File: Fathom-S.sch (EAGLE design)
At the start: 107 parts, among them IC1 LMH6643, IC2 LMH6643, IC3 ST490AB, IC4 ST490AB, IC5 FT230XS, Q1 BC817-40W, U1 MC7812, U2 MC7805, U4 INA139, U5 MC7805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

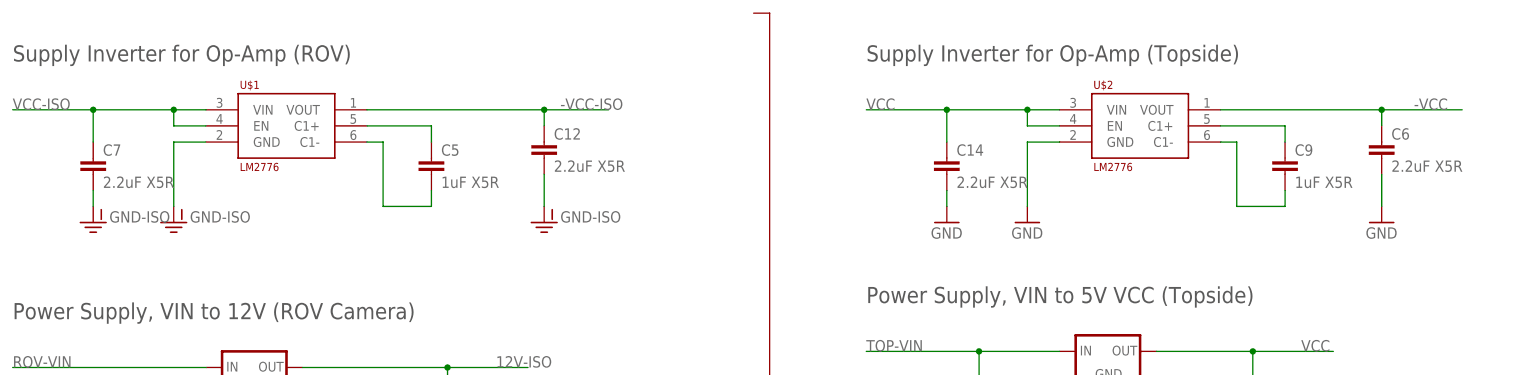
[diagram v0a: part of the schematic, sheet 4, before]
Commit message: Changed lm2776 components to match datasheet and hopefully fix our issues.
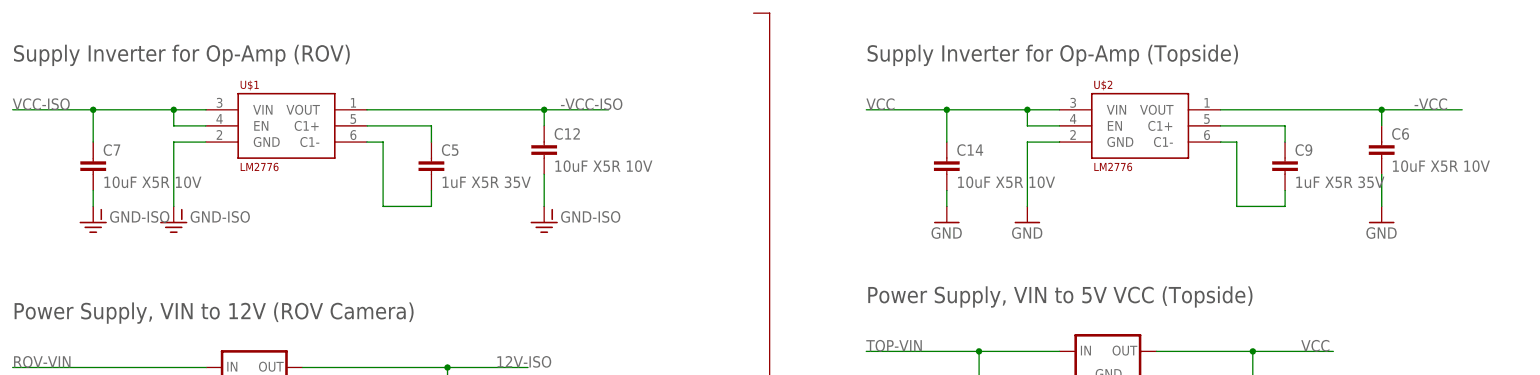
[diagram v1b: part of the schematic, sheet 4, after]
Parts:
- C12, C14, C6, C7: value 2.2uF X5R -> 10uF X5R 10V
- C5, C9: value 1uF X5R -> 1uF X5R 35V
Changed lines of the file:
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@@
 <part name="JP1" library="BR-Eagle-Library" deviceset="RCA" device="" value="PJRAN1X1U04X"/>
 <part name="U$1" library="BR-Eagle-Library" deviceset="LM2776" device=""/>
-<part name="C5" library="SparkFun-Passives" deviceset="CAP" device="0603-CAP" value="1uF X5R"/>
-<part name="C7" library="SparkFun-Passives" deviceset="CAP" device="0603-CAP" value="2.2uF X5R"/>
+<part name="C5" library="SparkFun-Passives" deviceset="CAP" device="0603-CAP" value="1uF X5R 35V"/>
+<part name="C7" library="SparkFun-Passives" deviceset="CAP" device="0603-CAP" value="10uF X5R 10V"/>
 <part name="C8" library="SparkFun-Passives" deviceset="CAP" device="0603-CAP" value="0.1uF"/>
 <part name="C10" library="SparkFun-Passives" deviceset="CAP_POL" device="1206" value="10uF 16V"/>
@@
 <part name="JP6" library="BR-Eagle-Library" deviceset="RCA" device="" value="PJRAN1X1U04X"/>
 <part name="U$2" library="BR-Eagle-Library" deviceset="LM2776" device=""/>
-<part name="C9" library="SparkFun-Passives" deviceset="CAP" device="0603-CAP" value="1uF X5R"/>
-<part name="C14" library="SparkFun-Passives" deviceset="CAP" device="0603-CAP" value="2.2uF X5R"/>
+<part name="C9" library="SparkFun-Passives" deviceset="CAP" device="0603-CAP" value="1uF X5R 35V"/>
+<part name="C14" library="SparkFun-Passives" deviceset="CAP" device="0603-CAP" value="10uF X5R 10V"/>
 <part name="GND12" library="SparkFun-Aesthetics" deviceset="GND" device=""/>
 <part name="GND13" library="SparkFun-Aesthetics" deviceset="GND" device=""/>
@@
 <part name="R17" library="SparkFun" deviceset="RESISTOR" device="0603-RES" value="10K"/>
 <part name="SJ4" library="SparkFun-Passives" deviceset="JUMPER-PAD-2-NC_BY_PASTE" device=""/>
-<part name="C6" library="SparkFun-Passives" deviceset="CAP" device="0603-CAP" value="2.2uF X5R"/>
-<part name="C12" library="SparkFun-Passives" deviceset="CAP" device="0603-CAP" value="2.2uF X5R"/>
+<part name="C6" library="SparkFun-Passives" deviceset="CAP" device="0603-CAP" value="10uF X5R 10V"/>
+<part name="C12" library="SparkFun-Passives" deviceset="CAP" device="0603-CAP" value="10uF X5R 10V"/>
 </parts>
 <sheets>

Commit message: Layout 'typos' fixed.
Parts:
- C12, C14, C6, C7: device SparkFun-Passives:CAP0603-CAP -> SparkFun-Passives:CAP0805
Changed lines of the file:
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@@
 <grid distance="0.1" unitdist="inch" unit="inch" style="lines" multiple="1" display="no" altdistance="0.01" altunitdist="inch" altunit="inch"/>
 <layers>
-<layer number="1" name="Top" color="4" fill="1" visible="no" active="no"/>
-<layer number="2" name="Route2" color="1" fill="3" visible="no" active="no"/>
-<layer number="3" name="Route3" color="4" fill="3" visible="no" active="no"/>
-<layer number="14" name="Route14" color="1" fill="6" visible="no" active="no"/>
-<layer number="15" name="Route15" color="4" fill="6" visible="no" active="no"/>
-<layer number="16" name="Bottom" color="1" fill="1" visible="no" active="no"/>
-<layer number="17" name="Pads" color="2" fill="1" visible="no" active="no"/>
-<layer number="18" name="Vias" color="2" fill="1" visible="no" active="no"/>
-<layer number="19" name="Unrouted" color="6" fill="1" visible="no" active="no"/>
-<layer number="20" name="Dimension" color="15" fill="1" visible="no" active="no"/>
-<layer number="21" name="tPlace" color="7" fill="1" visible="no" active="no"/>
-<layer number="22" name="bPlace" color="7" fill="1" visible="no" active="no"/>
-<layer number="23" name="tOrigins" color="15" fill="1" visible="no" active="no"/>
-<layer number="24" name="bOrigins" color="15" fill="1" visible="no" active="no"/>
-<layer number="25" name="tNames" color="7" fill="1" visible="no" active="no"/>
-<layer number="26" name="bNames" color="7" fill="1" visible="no" active="no"/>
-<layer number="27" name="tValues" color="7" fill="1" visible="no" active="no"/>
-<layer number="28" name="bValues" color="7" fill="1" visible="no" active="no"/>
+<layer number="1" name="Top" color="4" fill="1" visible="yes" active="no"/>
+<layer number="2" name="Route2" color="1" fill="3" visible="yes" active="no"/>
+<layer number="3" name="Route3" color="4" fill="3" visible="yes" active="no"/>
+<layer number="14" name="Route14" color="1" fill="6" visible="yes" active="no"/>
+<layer number="15" name="Route15" color="4" fill="6" visible="yes" active="no"/>
+<layer number="16" name="Bottom" color="1" fill="1" visible="yes" active="no"/>
+<layer number="17" name="Pads" color="2" fill="1" visible="yes" active="no"/>
+<layer number="18" name="Vias" color="2" fill="1" visible="yes" active="no"/>
+<layer number="19" name="Unrouted" color="6" fill="1" visible="yes" active="no"/>
+<layer number="20" name="Dimension" color="15" fill="1" visible="yes" active="no"/>
+<layer number="21" name="tPlace" color="7" fill="1" visible="yes" active="no"/>
+<layer number="22" name="bPlace" color="7" fill="1" visible="yes" active="no"/>
+<layer number="23" name="tOrigins" color="15" fill="1" visible="yes" active="no"/>
+<layer number="24" name="bOrigins" color="15" fill="1" visible="yes" active="no"/>
+<layer number="25" name="tNames" color="7" fill="1" visible="yes" active="no"/>
+<layer number="26" name="bNames" color="7" fill="1" visible="yes" active="no"/>
+<layer number="27" name="tValues" color="7" fill="1" visible="yes" active="no"/>
+<layer number="28" name="bValues" color="7" fill="1" visible="yes" active="no"/>
 <layer number="29" name="tStop" color="7" fill="3" visible="no" active="no"/>
 <layer number="30" name="bStop" color="7" fill="6" visible="no" active="no"/>
@@
 <layer number="35" name="tGlue" color="7" fill="4" visible="no" active="no"/>
 <layer number="36" name="bGlue" color="7" fill="5" visible="no" active="no"/>
-<layer number="37" name="tTest" color="7" fill="1" visible="no" active="no"/>
-<layer number="38" name="bTest" color="7" fill="1" visible="no" active="no"/>
+<layer number="37" name="tTest" color="7" fill="1" visible="yes" active="no"/>
+<layer number="38" name="bTest" color="7" fill="1" visible="yes" active="no"/>
 <layer number="39" name="tKeepout" color="4" fill="11" visible="no" active="no"/>
 <layer number="40" name="bKeepout" color="1" fill="11" visible="no" active="no"/>
@@
 <layer number="44" name="Drills" color="7" fill="1" visible="no" active="no"/>
 <layer number="45" name="Holes" color="7" fill="1" visible="no" active="no"/>
-<layer number="46" name="Milling" color="3" fill="1" visible="no" active="no"/>
-<layer number="47" name="Measures" color="7" fill="1" visible="no" active="no"/>
-<layer number="48" name="Document" color="7" fill="1" visible="no" active="no"/>
-<layer number="49" name="Reference" color="7" fill="1" visible="no" active="no"/>
-<layer number="50" name="dxf" color="7" fill="1" visible="no" active="no"/>
-<layer number="51" name="tDocu" color="7" fill="1" visible="no" active="no"/>
-<layer number="52" name="bDocu" color="7" fill="1" visible="no" active="no"/>
-<layer number="53" name="tGND_GNDA" color="7" fill="9" visible="no" active="no"/>
-<layer number="54" name="bGND_GNDA" color="1" fill="9" visible="no" active="no"/>
-<layer number="56" name="wert" color="7" fill="1" visible="no" active="no"/>
-<layer number="57" name="tCAD" color="7" fill="1" visible="no" active="no"/>
+<layer number="46" name="Milling" color="3" fill="1" visible="yes" active="no"/>
+<layer number="47" name="Measures" color="7" fill="1" visible="yes" active="no"/>
+<layer number="48" name="Document" color="7" fill="1" visible="yes" active="no"/>
+<layer number="49" name="Reference" color="7" fill="1" visible="yes" active="no"/>
+<layer number="50" name="dxf" color="7" fill="1" visible="yes" active="no"/>
+<layer number="51" name="tDocu" color="7" fill="1" visible="yes" active="no"/>
+<layer number="52" name="bDocu" color="7" fill="1" visible="yes" active="no"/>
+<layer number="53" name="tGND_GNDA" color="7" fill="9" visible="yes" active="no"/>
+<layer number="54" name="bGND_GNDA" color="1" fill="9" visible="yes" active="no"/>
+<layer number="56" name="wert" color="7" fill="1" visible="yes" active="no"/>
+<layer number="57" name="tCAD" color="7" fill="1" visible="yes" active="no"/>
 <layer number="90" name="Modules" color="5" fill="1" visible="yes" active="yes"/>
 <layer number="91" name="Nets" color="2" fill="1" visible="yes" active="yes"/>
@@
 <part name="U$1" library="BR-Eagle-Library" deviceset="LM2776" device=""/>
 <part name="C5" library="SparkFun-Passives" deviceset="CAP" device="0603-CAP" value="1uF X5R 35V"/>
-<part name="C7" library="SparkFun-Passives" deviceset="CAP" device="0603-CAP" value="10uF X5R 10V"/>
+<part name="C7" library="SparkFun-Passives" deviceset="CAP" device="0805" value="10uF X5R 10V"/>
 <part name="C8" library="SparkFun-Passives" deviceset="CAP" device="0603-CAP" value="0.1uF"/>
 <part name="C10" library="SparkFun-Passives" deviceset="CAP_POL" device="1206" value="10uF 16V"/>
@@
 <part name="U$2" library="BR-Eagle-Library" deviceset="LM2776" device=""/>
 <part name="C9" library="SparkFun-Passives" deviceset="CAP" device="0603-CAP" value="1uF X5R 35V"/>
-<part name="C14" library="SparkFun-Passives" deviceset="CAP" device="0603-CAP" value="10uF X5R 10V"/>
+<part name="C14" library="SparkFun-Passives" deviceset="CAP" device="0805" value="10uF X5R 10V"/>
 <part name="GND12" library="SparkFun-Aesthetics" deviceset="GND" device=""/>
 <part name="GND13" library="SparkFun-Aesthetics" deviceset="GND" device=""/>
@@
 <part name="R17" library="SparkFun" deviceset="RESISTOR" device="0603-RES" value="10K"/>
 <part name="SJ4" library="SparkFun-Passives" deviceset="JUMPER-PAD-2-NC_BY_PASTE" device=""/>
-<part name="C6" library="SparkFun-Passives" deviceset="CAP" device="0603-CAP" value="10uF X5R 10V"/>
-<part name="C12" library="SparkFun-Passives" deviceset="CAP" device="0603-CAP" value="10uF X5R 10V"/>
+<part name="C6" library="SparkFun-Passives" deviceset="CAP" device="0805" value="10uF X5R 10V"/>
+<part name="C12" library="SparkFun-Passives" deviceset="CAP" device="0805" value="10uF X5R 10V"/>
 </parts>
 <sheets>

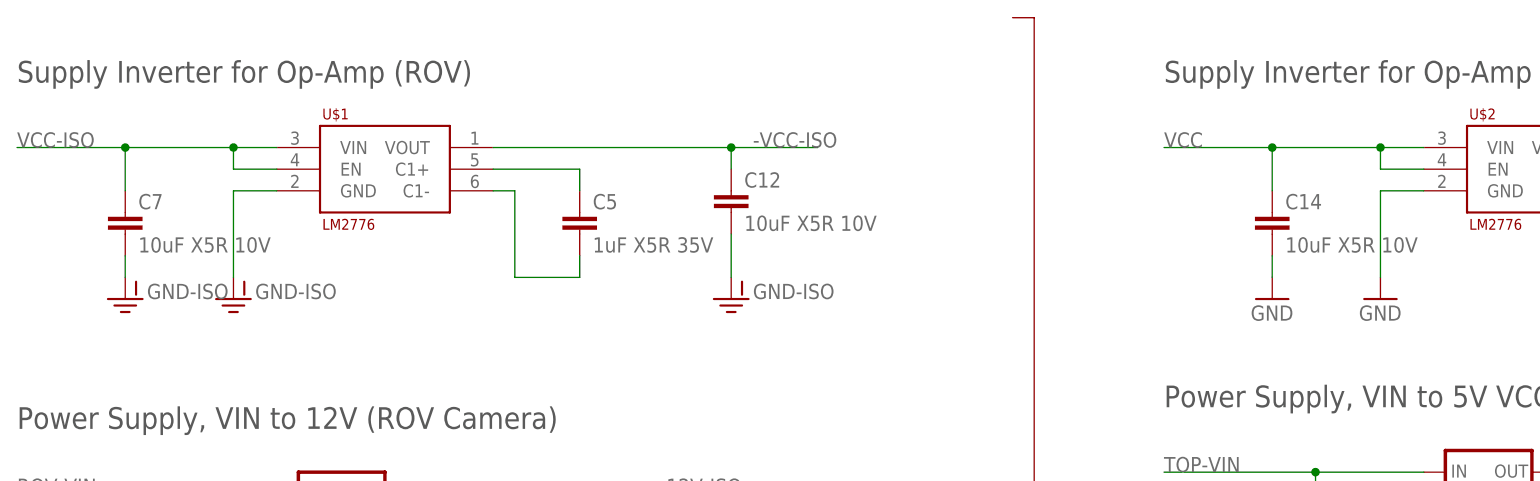
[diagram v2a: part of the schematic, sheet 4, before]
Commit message: Redid the layout for the video amplifiers and supply inverters to help fix recent issues. There is now an analog ground plane. LM2776 are laid out almost identical to the eval board.
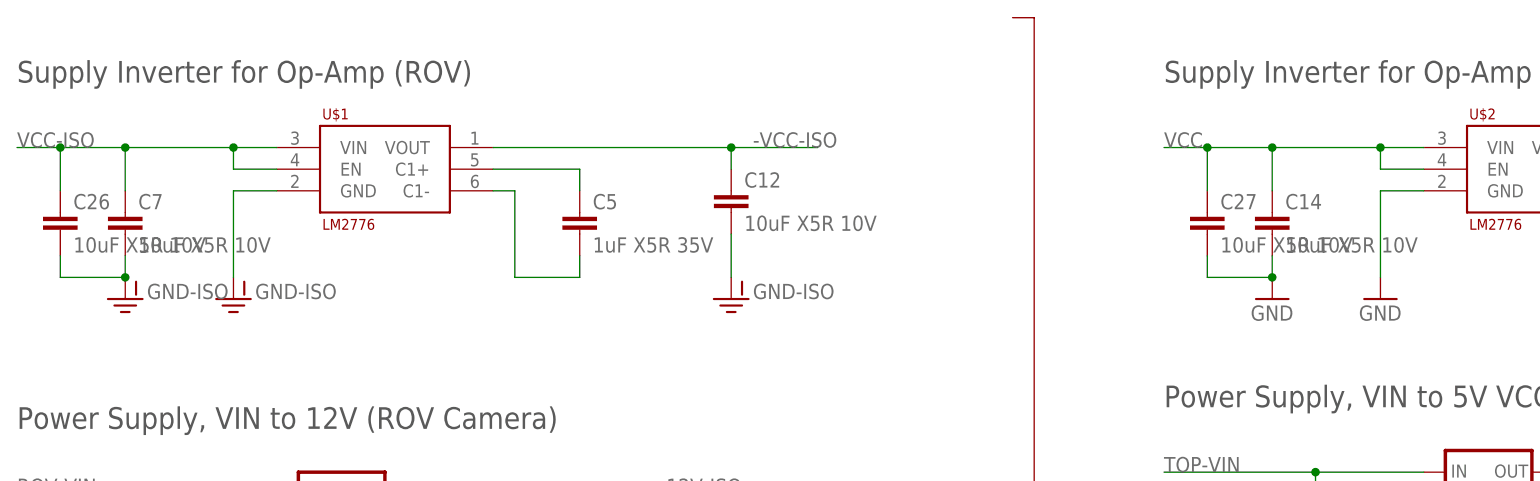
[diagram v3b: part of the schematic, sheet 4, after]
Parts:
- added C26, C27: 10uF X5R 10V, SparkFun-Passives:CAP0805
- JP1, JP6: device BR-Eagle-Library:RCA -> BlueRobotics-Main:RCA
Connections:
- net GND: now also C27.2
- net GND-ISO: now also C26.2
- net VCC: now also C27.1
- net VCC-ISO: now also C26.1
